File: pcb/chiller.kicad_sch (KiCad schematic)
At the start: 49 parts, among them J1 Conn_01x03, J10 Current Sense, J11 Display, J12 Debug, J13 Conn_01x04, J14 Flow sensor, J15 Fan, J2 Conn_01x03, J3 Ext, J4 Conn_01x02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

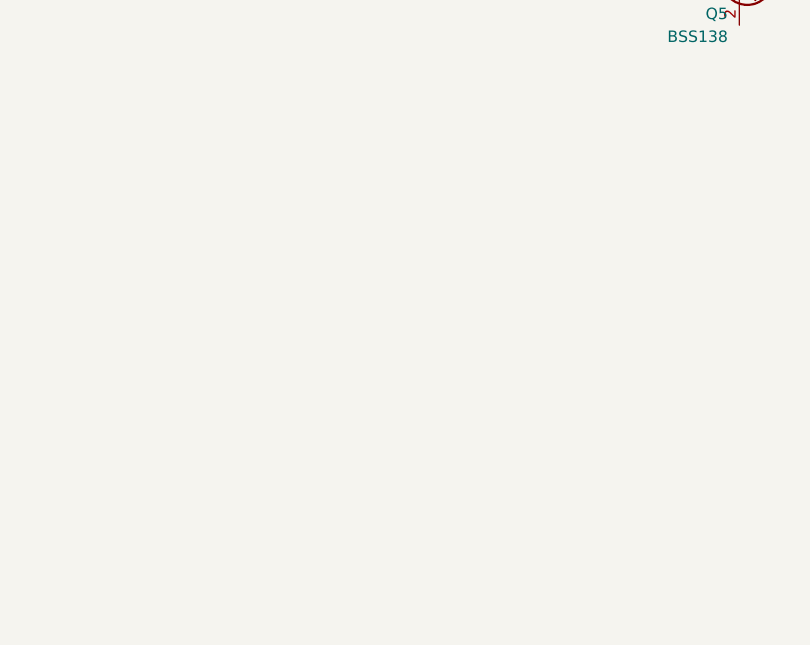
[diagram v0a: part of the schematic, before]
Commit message: Add LEDs.
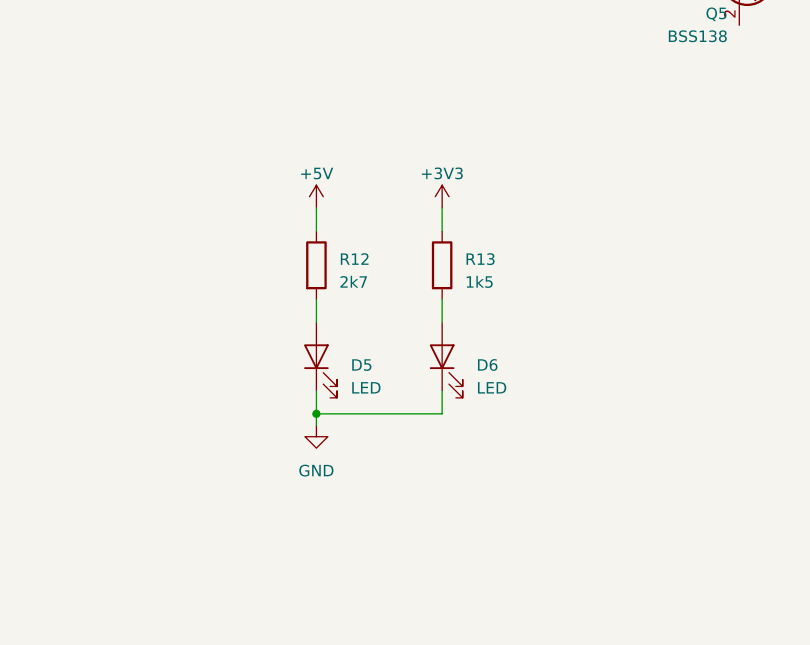
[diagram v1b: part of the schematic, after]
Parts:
- added D5, D6: LED, LED_SMD:LED_0603_1608Metric, symbol Device:LED
- added R12: 2k7, Resistor_SMD:R_0603_1608Metric, symbol Device:R
- added R13: 1k5, Resistor_SMD:R_0603_1608Metric, symbol Device:R
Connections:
- net +3V3: now also R13.1
- net +5V: now also R12.1
- net GND: now also D5.1 (K), D6.1 (K)
- new net: D5.2 (A), R12.2
- new net: D6.2 (A), R13.2
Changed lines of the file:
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@@
   (junction (at 123.19 166.37) (diameter 0) (color 0 0 0 0)
+  )
+  (junction (at 237.49 165.1) (diameter 0) (color 0 0 0 0)
   )
   (junction (at 24.13 78.74) (diameter 0) (color 0 0 0 0)
@@
     (stroke (width 0) (type default))
   )
+  (wire (pts (xy 237.49 165.1) (xy 237.49 166.37))
+    (stroke (width 0) (type default))
+  )
   (wire (pts (xy 167.64 217.17) (xy 167.64 222.25))
     (stroke (width 0) (type default))
@@
     (stroke (width 0) (type default))
   )
+  (wire (pts (xy 251.46 165.1) (xy 251.46 162.56))
+    (stroke (width 0) (type default))
+  )
   (wire (pts (xy 161.29 44.45) (xy 161.29 45.72))
     (stroke (width 0) (type default))
@@
     (stroke (width 0) (type default))
   )
+  (wire (pts (xy 237.49 162.56) (xy 237.49 165.1))
+    (stroke (width 0) (type default))
+  )
   (wire (pts (xy 88.9 46.99) (xy 93.98 46.99))
     (stroke (width 0) (type default))
@@
     (stroke (width 0) (type default))
   )
+  (wire (pts (xy 237.49 165.1) (xy 251.46 165.1))
+    (stroke (width 0) (type default))
+  )
   (wire (pts (xy 173.99 161.29) (xy 173.99 165.1))
     (stroke (width 0) (type default))
@@
     (stroke (width 0) (type default))
   )
+  (wire (pts (xy 251.46 142.24) (xy 251.46 144.78))
+    (stroke (width 0) (type default))
+  )
   (wire (pts (xy 124.46 152.4) (xy 120.65 152.4))
     (stroke (width 0) (type default))
@@
     (stroke (width 0) (type solid))
   )
+  (wire (pts (xy 237.49 152.4) (xy 237.49 154.94))
+    (stroke (width 0) (type default))
+  )
   (wire (pts (xy 57.15 119.38) (xy 64.77 119.38))
     (stroke (width 0) (type default))
@@
   )
   (wire (pts (xy 243.84 87.63) (xy 243.84 88.9))
+    (stroke (width 0) (type default))
+  )
+  (wire (pts (xy 251.46 152.4) (xy 251.46 154.94))
     (stroke (width 0) (type default))
   )
@@
   )
   (wire (pts (xy 245.11 39.37) (xy 246.38 39.37))
+    (stroke (width 0) (type default))
+  )
+  (wire (pts (xy 237.49 142.24) (xy 237.49 144.78))
     (stroke (width 0) (type default))
   )
@@
         (path "/212a0d71-cc7b-49f8-b4ca-a935e5355dca"
           (reference "#PWR012") (unit 1)
+        )
+      )
+    )
+  )
+  (symbol (lib_id "Device:R") (at 237.49 148.59 0) (unit 1)
+    (in_bom yes) (on_board yes) (dnp no) (fields_autoplaced)
+    (property "Reference" "R12" (at 240.03 147.955 0)
+      (effects (font (size 1.27 1.27)) (justify left))
+    )
+    (property "Value" "2k7" (at 240.03 150.495 0)
+      (effects (font (size 1.27 1.27)) (justify left))
+    )
+    (property "Footprint" "Resistor_SMD:R_0603_1608Metric" (at 235.712 148.59 90)
+      (effects (font (size 1.27 1.27)) hide)
+    )
+    (property "Datasheet" "~" (at 237.49 148.59 0)
+      (effects (font (size 1.27 1.27)) hide)
+    )
+    (pin "1")
+    (pin "2")
+    (instances
+      (project "chiller"
+        (path "/212a0d71-cc7b-49f8-b4ca-a935e5355dca"
+          (reference "R12") (unit 1)
+        )
+      )
+    )
+  )
+  (symbol (lib_id "power:+5V") (at 237.49 142.24 0) (unit 1)
+    (in_bom yes) (on_board yes) (dnp no) (fields_autoplaced)
+    (property "Reference" "#PWR031" (at 237.49 146.05 0)
+      (effects (font (size 1.27 1.27)) hide)
+    )
+    (property "Value" "+5V" (at 237.49 138.43 0)
+      (effects (font (size 1.27 1.27)))
+    )
+    (property "Footprint" "" (at 237.49 142.24 0)
+      (effects (font (size 1.27 1.27)) hide)
+    )
+    (property "Datasheet" "" (at 237.49 142.24 0)
+      (effects (font (size 1.27 1.27)) hide)
+    )
+    (pin "1")
+    (instances
+      (project "chiller"
+        (path "/212a0d71-cc7b-49f8-b4ca-a935e5355dca"
+          (reference "#PWR031") (unit 1)
         )
       )
@@
     )
   )
+  (symbol (lib_id "Device:LED") (at 237.49 158.75 90) (unit 1)
+    (in_bom yes) (on_board yes) (dnp no) (fields_autoplaced)
+    (property "Reference" "D5" (at 241.3 159.7152 90)
+      (effects (font (size 1.27 1.27)) (justify right))
+    )
+    (property "Value" "LED" (at 241.3 162.2552 90)
+      (effects (font (size 1.27 1.27)) (justify right))
+    )
+    (property "Footprint" "LED_SMD:LED_0603_1608Metric" (at 237.49 158.75 0)
+      (effects (font (size 1.27 1.27)) hide)
+    )
+    (property "Datasheet" "~" (at 237.49 158.75 0)
+      (effects (font (size 1.27 1.27)) hide)
+    )
+    (pin "1")
+    (pin "2")
+    (instances
+      (project "chiller"
+        (path "/212a0d71-cc7b-49f8-b4ca-a935e5355dca"
+          (reference "D5") (unit 1)
+        )
+      )
+    )
+  )
   (symbol (lib_id "Device:R_Small") (at 165.1 85.09 0) (mirror y) (unit 1)
     (in_bom yes) (on_board yes) (dnp no)
@@
     )
   )
+  (symbol (lib_id "power:GND") (at 237.49 166.37 0) (unit 1)
+    (in_bom yes) (on_board yes) (dnp no) (fields_autoplaced)
+    (property "Reference" "#PWR033" (at 237.49 172.72 0)
+      (effects (font (size 1.27 1.27)) hide)
+    )
+    (property "Value" "GND" (at 237.49 171.45 0)
+      (effects (font (size 1.27 1.27)))
+    )
+    (property "Footprint" "" (at 237.49 166.37 0)
+      (effects (font (size 1.27 1.27)) hide)
+    )
+    (property "Datasheet" "" (at 237.49 166.37 0)
+      (effects (font (size 1.27 1.27)) hide)
+    )
+    (pin "1")
+    (instances
+      (project "chiller"
+        (path "/212a0d71-cc7b-49f8-b4ca-a935e5355dca"
+          (reference "#PWR033") (unit 1)
+        )
+      )
+    )
+  )
   (symbol (lib_id "power:GND") (at 252.73 50.8 0) (unit 1)
     (in_bom yes) (on_board yes) (dnp no) (fields_autoplaced)
@@
     )
   )
+  (symbol (lib_id "Device:LED") (at 251.46 158.75 90) (unit 1)
+    (in_bom yes) (on_board yes) (dnp no) (fields_autoplaced)
+    (property "Reference" "D6" (at 255.27 159.7152 90)
+      (effects (font (size 1.27 1.27)) (justify right))
+    )
+    (property "Value" "LED" (at 255.27 162.2552 90)
+      (effects (font (size 1.27 1.27)) (justify right))
+    )
+    (property "Footprint" "LED_SMD:LED_0603_1608Metric" (at 251.46 158.75 0)
+      (effects (font (size 1.27 1.27)) hide)
+    )
+    (property "Datasheet" "~" (at 251.46 158.75 0)
+      (effects (font (size 1.27 1.27)) hide)
+    )
+    (pin "1")
+    (pin "2")
+    (instances
+      (project "chiller"
+        (path "/212a0d71-cc7b-49f8-b4ca-a935e5355dca"
+          (reference "D6") (unit 1)
+        )
+      )
+    )
+  )
   (symbol (lib_id "Connector_Generic:Conn_01x02") (at 116.84 213.36 0) (mirror y) (unit 1)
     (in_bom yes) (on_board yes) (dnp no)
@@
         (path "/212a0d71-cc7b-49f8-b4ca-a935e5355dca"
           (reference "#PWR05") (unit 1)
+        )
+      )
+    )
+  )
+  (symbol (lib_id "Device:R") (at 251.46 148.59 0) (unit 1)
+    (in_bom yes) (on_board yes) (dnp no) (fields_autoplaced)
+    (property "Reference" "R13" (at 254 147.955 0)
+      (effects (font (size 1.27 1.27)) (justify left))
+    )
+    (property "Value" "1k5" (at 254 150.495 0)
+      (effects (font (size 1.27 1.27)) (justify left))
+    )
+    (property "Footprint" "Resistor_SMD:R_0603_1608Metric" (at 249.682 148.59 90)
+      (effects (font (size 1.27 1.27)) hide)
+    )
+    (property "Datasheet" "~" (at 251.46 148.59 0)
+      (effects (font (size 1.27 1.27)) hide)
+    )
+    (pin "1")
+    (pin "2")
+    (instances
+      (project "chiller"
+        (path "/212a0d71-cc7b-49f8-b4ca-a935e5355dca"
+          (reference "R13") (unit 1)
         )
       )
@@
         )
       )
+    )
+  )
+  (symbol (lib_id "power:+3V3") (at 251.46 142.24 0) (unit 1)
+    (in_bom yes) (on_board yes) (dnp no) (fields_autoplaced)
+    (property "Reference" "#PWR032" (at 251.46 146.05 0)
+      (effects (font (size 1.27 1.27)) hide)
+    )
+    (property "Value" "+3V3" (at 251.46 138.43 0)
+      (effects (font (size 1.27 1.27)))
+    )
+    (property "Footprint" "" (at 251.46 142.24 0)
+      (effects (font (size 1.27 1.27)) hide)
+    )
+    (property "Datasheet" "" (at 251.46 142.24 0)
+      (effects (font (size 1.27 1.27)) hide)
+    )
+    (pin "1")
+    (instances
+      (project "chiller"
+        (path "/212a0d71-cc7b-49f8-b4ca-a935e5355dca"
+          (reference "#PWR032") (unit 1)
+        )
+      )

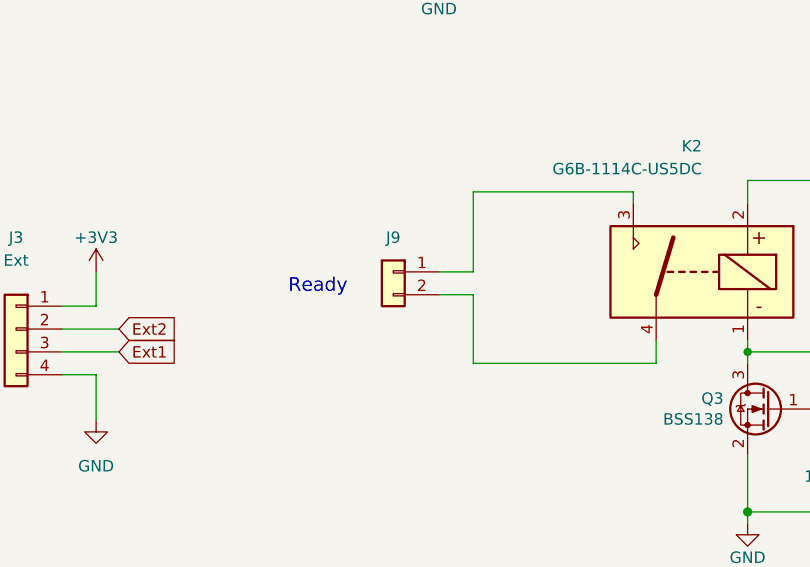
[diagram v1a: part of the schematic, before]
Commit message: Move J9.
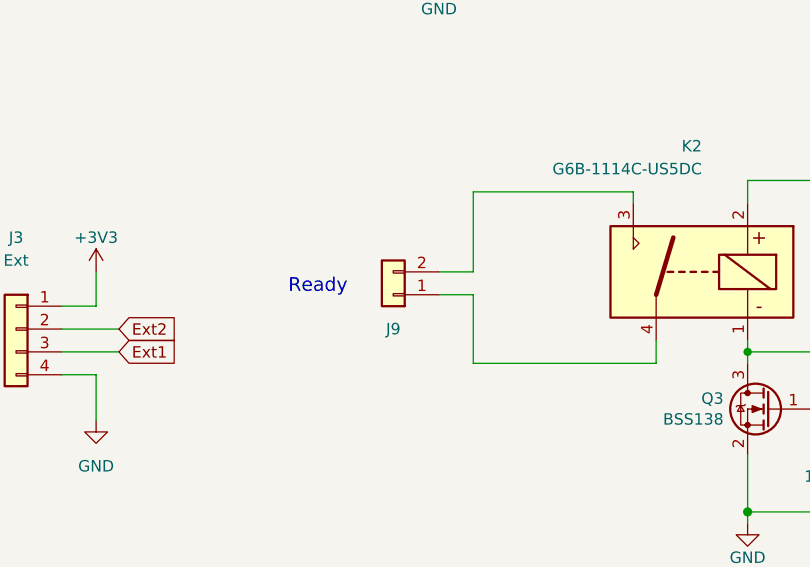
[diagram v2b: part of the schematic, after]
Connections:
- net at J9.1 (Pin_1): now also K2.4; no longer K2.3
- net at J9.2 (Pin_2): now also K2.3; no longer K2.4
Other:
- moved on the sheet: J9
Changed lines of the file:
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@@
     )
   )
-  (symbol (lib_id "Connector_Generic:Conn_01x02") (at 116.84 213.36 0) (mirror y) (unit 1)
+  (symbol (lib_id "Connector_Generic:Conn_01x02") (at 116.84 215.9 180) (unit 1)
     (in_bom yes) (on_board yes) (dnp no)
-    (property "Reference" "J9" (at 116.84 209.55 0)
+    (property "Reference" "J9" (at 116.84 219.71 0)
       (effects (font (size 1.27 1.27)))
     )
-    (property "Value" "CONN_01X02" (at 114.3 213.36 90)
+    (property "Value" "CONN_01X02" (at 114.3 215.9 90)
       (effects (font (size 1.27 1.27)) hide)
     )
-    (property "Footprint" "Connector_JST:JST_XH_B2B-XH-A_1x02_P2.50mm_Vertical" (at 116.84 213.36 0)
+    (property "Footprint" "Connector_JST:JST_XH_B2B-XH-A_1x02_P2.50mm_Vertical" (at 116.84 215.9 0)
       (effects (font (size 1.27 1.27)) hide)
     )
-    (property "Datasheet" "~" (at 116.84 213.36 0)
+    (property "Datasheet" "~" (at 116.84 215.9 0)
       (effects (font (size 1.27 1.27)) hide)
     )
